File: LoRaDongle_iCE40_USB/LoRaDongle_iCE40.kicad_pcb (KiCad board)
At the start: 4 copper layers, 110 x 45 mm, 129 parts, among them IC1 93LC56BT-I_OT, IC2 ICE40UP5K-UWG30ITR1K, IC3 N25Q032A13ESC40F, J1 USB_A, J2 Conn_01x08, J3 Conn_02x02_Top_Bottom, J4 Jumper, J5 142-0701-801, J6 Conn_01x06, J7 Jumper_NC_Small, J8 Jumper, J9 Conn_02x02_Top_Bottom, SW1 SW_Push, U1 RP550K0001A-TR, U2 FT232H, U3 SX1261IMLTRT, U4 SKY13587-378LF, X1 ECS-2520MV-500-BL-TR, Y1 Crystal_GND24_Small, Y2 Crystal

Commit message: first traces laid
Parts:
- moved C18 1.89 mm to (127.1, 101.4), turned to 0 degrees
- moved C21 1.83 mm to (138.3, 102.5)
- moved C22 1.83 mm to (137.2, 102.5)
- moved R8 1.57 mm to (141.0, 94.7)
- moved C13 1.13 mm to (139.2, 91.0)
- moved C16 1.13 mm to (138.2, 91.0)
- moved C20 0.98 mm to (127.1, 100.4), turned to 0 degrees
- moved C8 0.66 mm to (129.8, 82.5), turned to 0 degrees
- moved C17 0.35 mm to (135.8, 90.2)
- moved C24 0.17 mm to (158.7, 100.9)
- moved C27 0.17 mm to (159.7, 100.9)
- moved C25 0.13 mm to (153.5, 100.9)
- moved C26 0.13 mm to (152.4, 100.9)
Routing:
- net GND: track 0.00 -> 51.1 mm, vias 0 -> 13
- net 3V3: track 0.00 -> 19.0 mm, vias 0 -> 5
- net /USB_Interface/CS#: track 0.00 -> 17.1 mm, vias 0 -> 2
- net /USB_Interface/CLK: track 0.00 -> 14.1 mm, vias 0 -> 2
- net /USB_Interface/VPLL: track 0.00 -> 13.2 mm
- net /USB_Interface/VPHY: track 0.00 -> 13.2 mm
- net /USB_Interface/DATA: track 0.00 -> 8.67 mm
- net Net-(C37-Pad2): track 0.00 -> 7.66 mm
- net /RF Circuitry/DIO2: track 0.00 -> 5.84 mm, vias 0 -> 1
- net Net-(C49-Pad2): track 0.00 -> 5.63 mm
- net /ice40up5k_circuit/ANTENNA_SW: track 0.00 -> 5.27 mm, vias 0 -> 1
- net Net-(C13-Pad1): track 0.00 -> 4.13 mm
- net Net-(C16-Pad1): track 0.00 -> 3.85 mm
- net /USB_Interface/~RESET: track 0.00 -> 3.82 mm
- net /RF Circuitry/VCTL1: track 0.00 -> 3.78 mm
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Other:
- rule trace_min: 0.15 -> 0.1

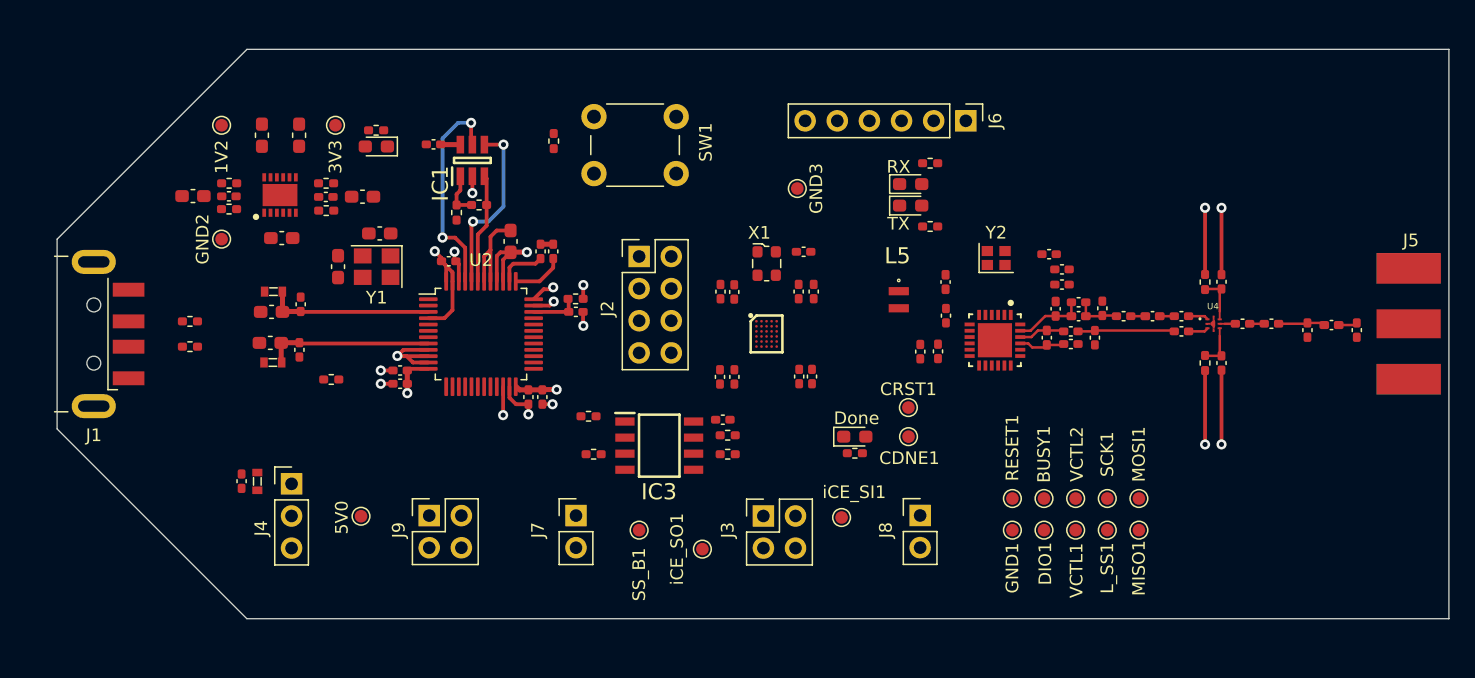
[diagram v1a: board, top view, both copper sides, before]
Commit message: added more traces
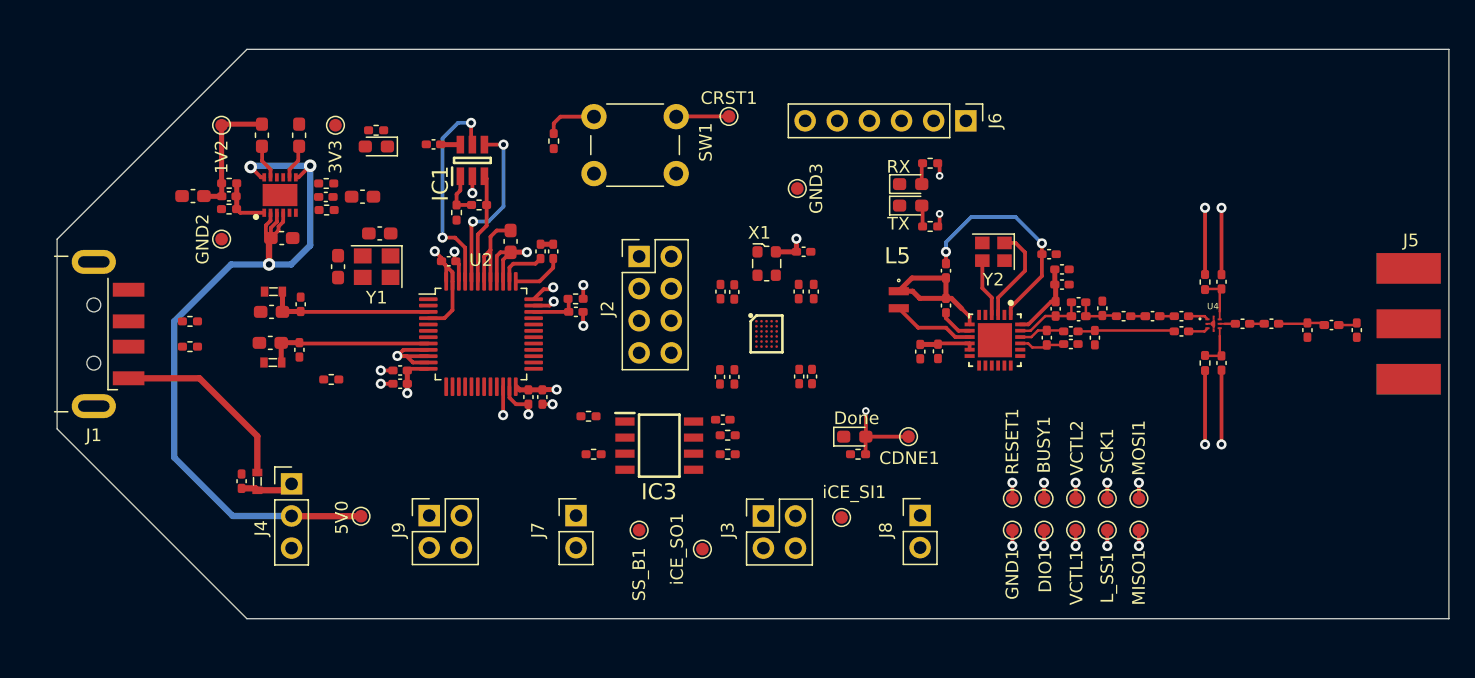
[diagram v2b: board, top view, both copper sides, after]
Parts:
- Y2: value Crystal -> Crystal_GND24; footprint Crystal:Crystal_SMD_2016-4Pin_2.0x1.6mm -> Crystal:Crystal_SMD_2520-4Pin_2.5x2.0mm
- moved CRST1 27.0 mm to (153.1, 80.3)
- moved R4 2.15 mm to (121.3, 85.6)
- moved R5 2.11 mm to (121.3, 87.7)
- moved L3 0.89 mm to (170.2, 92.5)
- moved C42 0.80 mm to (170.2, 95.2)
- moved Y2 0.54 mm to (174.0, 91.0), turned to 180 degrees
- moved R12 0.26 mm to (163.3, 107.0)
- turned R21 to 180 degrees
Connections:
- Y2 pad 1: Net-(U3-Pad4) -> Net-(U3-Pad3)
- Y2 pad 2: Net-(U3-Pad3) -> GND
- Y2 pad 3: (no net) -> Net-(U3-Pad4)
- Y2 pad 4: (no net) -> GND
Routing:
- net +5V: track 0.00 -> 63.7 mm, vias 0 -> 3
- net Net-(C35-Pad1): track 0.00 -> 17.6 mm, vias 0 -> 2
- net /VBUS: track 0.00 -> 14.9 mm
- net /RF Circuitry/VREG: track 0.00 -> 12.8 mm
- net 1V2: track 0.00 -> 10.3 mm
- net /ICE_CRESET: track 0.00 -> 8.38 mm
- net Net-(U3-Pad3): track 0.00 -> 7.76 mm
- net /ICE_CDONE: track 0.00 -> 6.80 mm, vias 0 -> 1
- net Net-(L5-Pad2): track 0.00 -> 6.54 mm
- net /RF Circuitry/VR_PA: track 0.00 -> 6.12 mm
- net Net-(U3-Pad4): track 0.00 -> 4.60 mm
- net RadioPower: track 0.00 -> 4.43 mm
- net Net-(C5-Pad1): track 0.00 -> 4.35 mm
- net /V_USB: track 0.00 -> 4.22 mm
- net GND: track 51.1 -> 55.1 mm, vias 13 -> 14
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
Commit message: breakout of bga part
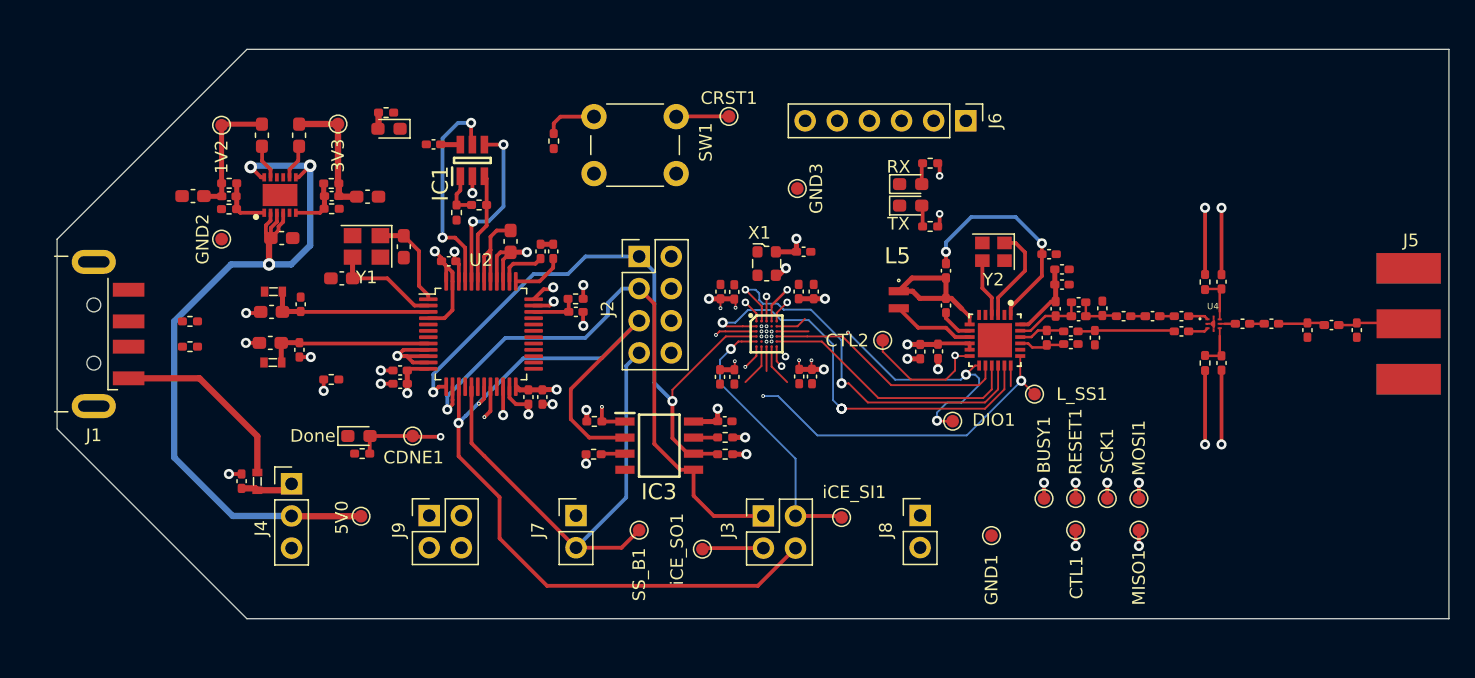
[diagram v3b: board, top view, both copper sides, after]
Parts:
- CTL1: renamed from VCTL1; value VCTL1 -> CTL1
- CTL2: renamed from VCTL2; value VCTL2 -> CTL2
- moved R12 39.2 mm to (124.1, 107.0)
- moved CDNE1 39.2 mm to (128.1, 105.6)
- moved D2 39.2 mm to (123.9, 105.6)
- moved CTL2 19.7 mm to (165.2, 98.0), turned to 90 degrees
- moved L_SS1 12.2 mm to (177.2, 102.2), turned to 180 degrees
- moved DIO1 11.2 mm to (170.8, 104.4), turned to 90 degrees
- moved RESET1 5.00 mm to (180.5, 110.5)
- moved C14 2.17 mm to (127.4, 90.6), turned to 270 degrees
- moved Y1 1.79 mm to (124.5, 90.6)
- moved D1 1.72 mm to (126.2, 81.3)
- moved GND1 1.71 mm to (173.8, 113.4)
- moved R3 1.60 mm to (126.0, 80.0)
- moved C15 0.97 mm to (122.5, 93.1), turned to 180 degrees
- moved R15 0.62 mm to (142.5, 104.4)
- moved C3 0.47 mm to (121.7, 86.6)
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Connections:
- J2 pad 1: /ICE_CRESET -> /SPI_SCK
- J2 pad 2: /ICE_CDONE -> /ICE_CRESET
- J2 pad 3: /SPI_SS -> /SPI_MOSI
- J2 pad 4: /SPI_MISO -> /ICE_CDONE
- J2 pad 5: /SPI_MOSI -> /SPI_MISO
- J2 pad 6: /SPI_SCK -> GND
- J2 pad 7: GND -> /SPI_SS
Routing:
- net /SPI_MISO: track 0.00 -> 72.0 mm, vias 0 -> 1
- net /SPI_SCK: track 1.25 -> 54.4 mm, vias 1 -> 3
- net /SPI_SS: track 0.00 -> 49.9 mm, vias 0 -> 1
- net /SPI_MOSI: track 0.00 -> 47.3 mm, vias 0 -> 1
- net /ICE_CDONE: track 6.80 -> 44.0 mm, vias 1 -> 4
- net /RF Circuitry/LoRa_MOSI: track 1.25 -> 35.0 mm, vias 1 -> 4
- net /ICE_CRESET: track 8.38 -> 41.9 mm, vias 0 -> 1
- net /RF Circuitry/LoRa_MISO: track 1.25 -> 32.5 mm, vias 1 -> 3
- net /RF Circuitry/LoRa_!SS: track 1.25 -> 31.9 mm, vias 1 -> 4
- net /RF Circuitry/DIO1: track 1.25 -> 26.7 mm, vias 1 -> 5
- net /ice40up5k_circuit/iCE_SO: track 0.00 -> 22.7 mm, vias 0 -> 1
- net /ice40up5k_circuit/iCE_SI: track 0.00 -> 22.0 mm, vias 0 -> 1
- net /ice40up5k_circuit/LoRa_~RESET: track 1.25 -> 22.3 mm
- net /RF Circuitry/BUSY: track 1.25 -> 20.6 mm
- net 3V3FPGA: track 0.00 -> 17.2 mm, vias 0 -> 8
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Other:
- net class Default: clearance 0.2 -> 0.1
- rule trace_clearance: 0.2 -> 0.1
- rule via_min_drill: 0.3 -> 0.1
- rule via_min_size: 0.4 -> 0.2

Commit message: added to other traces
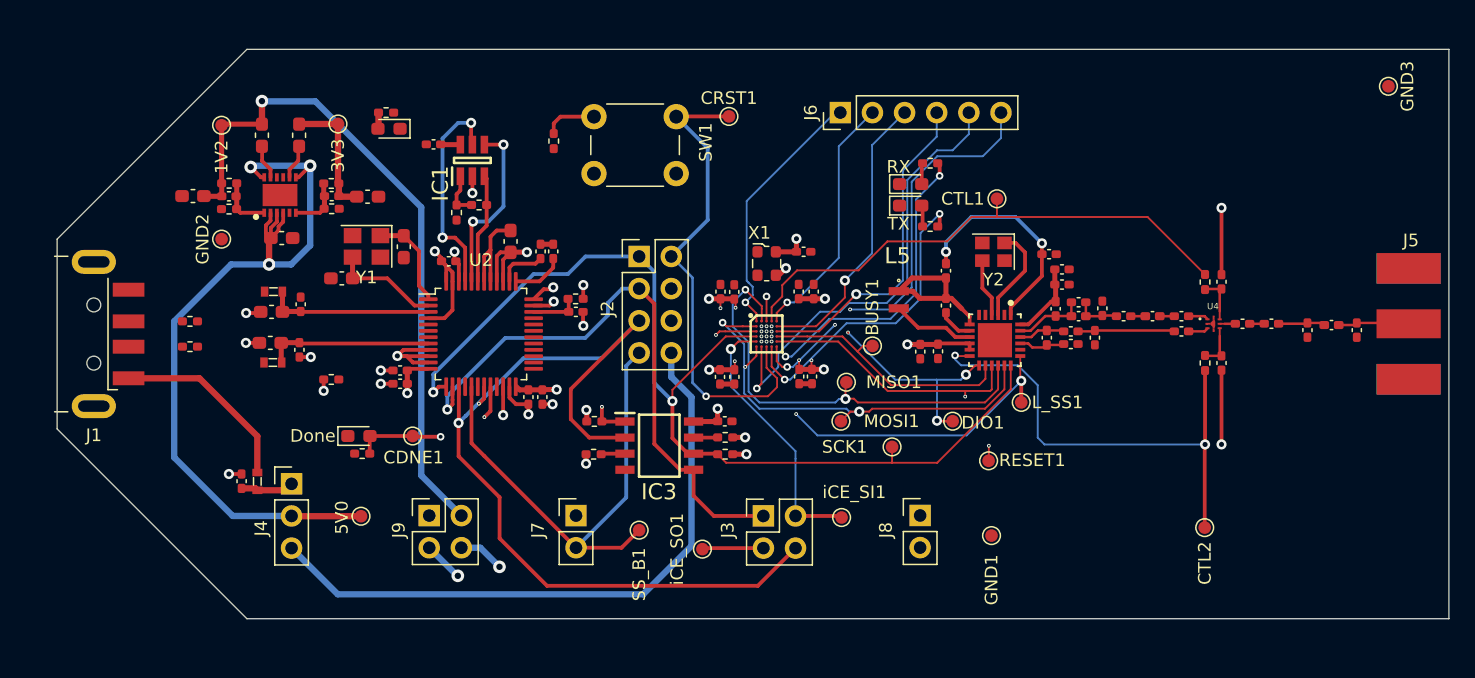
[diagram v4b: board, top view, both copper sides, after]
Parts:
- moved GND3 47.4 mm to (205.2, 77.9)
- moved CTL2 29.4 mm to (190.7, 112.8), turned to 180 degrees
- moved CTL1 26.9 mm to (174.3, 86.8), turned to 90 degrees
- moved MISO1 25.9 mm to (162.4, 101.3), turned to 180 degrees
- moved MOSI1 24.3 mm to (161.9, 104.4), turned to 0 degrees
- moved BUSY1 18.1 mm to (164.4, 98.4)
- moved SCK1 17.5 mm to (166.0, 106.4), turned to 90 degrees
- moved J6 9.94 mm to (161.9, 80.0), turned to 90 degrees
- moved RESET1 7.50 mm to (173.6, 107.5), turned to 90 degrees
- moved L_SS1 1.23 mm to (176.2, 102.9)
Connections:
- net /USB_Interface/~RESET renamed /USB_Interface/~{RESET}
- net /ice40up5k_circuit/ANTENNA_SW renamed /RF Circuitry/ANT_SW
- net /ice40up5k_circuit/LoRa_~RESET renamed /RF Circuitry/~{RESET}
- IC2 pad A5: /ice40up5k_circuit/Pin_3 -> /ice40up5k_circuit/Pin_1
- IC2 pad B5: /ice40up5k_circuit/Pin_4 -> /ice40up5k_circuit/Pin_2
- IC2 pad C5: /ice40up5k_circuit/Pin_5 -> /ice40up5k_circuit/Pin_3
- IC2 pad F2: /ice40up5k_circuit/Pin_2 -> /ice40up5k_circuit/Pin_4
- IC2 pad F5: /ice40up5k_circuit/Pin_1 -> /ice40up5k_circuit/Pin_5
- J1 pad 5: Net-(J1-Pad5) -> unconnected-(J1-Pad5)
- J8 pad 1: 3V3 -> RadioPower
- J8 pad 2: RadioPower -> 3V3
- U2 pad 16: Net-(U2-Pad16) -> unconnected-(U2-Pad16)
- U2 pad 18: Net-(U2-Pad18) -> unconnected-(U2-Pad18)
- U2 pad 21: Net-(U2-Pad21) -> unconnected-(U2-Pad21)
- U2 pad 25: Net-(U2-Pad25) -> unconnected-(U2-Pad25)
- U2 pad 26: Net-(U2-Pad26) -> unconnected-(U2-Pad26)
- U2 pad 27: Net-(U2-Pad27) -> unconnected-(U2-Pad27)
- U2 pad 28: Net-(U2-Pad28) -> unconnected-(U2-Pad28)
- U2 pad 29: Net-(U2-Pad29) -> unconnected-(U2-Pad29)
- U2 pad 30: Net-(U2-Pad30) -> unconnected-(U2-Pad30)
- U2 pad 31: Net-(U2-Pad31) -> unconnected-(U2-Pad31)
- U2 pad 32: Net-(U2-Pad32) -> unconnected-(U2-Pad32)
- U2 pad 33: Net-(U2-Pad33) -> unconnected-(U2-Pad33)
- U4 pad 4: /RF Circuitry/VCTL2 -> /RF Circuitry/CTL2
- U4 pad 6: /RF Circuitry/VCTL1 -> /RF Circuitry/CTL1
- X1 pad 1: Net-(X1-Pad1) -> unconnected-(X1-Pad1)
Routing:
- net 1V2FPGA: track 12.2 -> 80.0 mm, vias 6 -> 7
- net 3V3FPGA: track 17.2 -> 79.7 mm, vias 8 -> 10
- net /V_conn: track 0.00 -> 50.6 mm
- net 1V2: track 10.3 -> 53.8 mm, vias 0 -> 1
- net /ice40up5k_circuit/Pin_4: track 2.47 -> 35.6 mm, vias 0 -> 1
- net /ICE_CRESET: track 41.9 -> 74.9 mm, vias 1 -> 2
- net /RF Circuitry/ANT_SW: track 9.52 -> 42.2 mm, vias 3 -> 0
- net /ice40up5k_circuit/Pin_5: track 2.52 -> 33.5 mm, vias 0 -> 3
- net /SPI_SCK: track 54.4 -> 80.6 mm, vias 3 -> 2
- net /ice40up5k_circuit/Pin_3: track 1.83 -> 26.0 mm
- net /RF Circuitry/DIO2: track 16.0 -> 38.9 mm
- net /RF Circuitry/RX_LED: track 2.71 -> 25.2 mm
- net /RF Circuitry/TX_LED: track 4.38 -> 24.8 mm, vias 1 -> 2
- net /ice40up5k_circuit/Pin_2: track 3.34 -> 22.9 mm, vias 0 -> 1
- net /ice40up5k_circuit/Pin_0: track 1.85 -> 20.6 mm
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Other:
- net class Default removed

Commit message: added copper pours
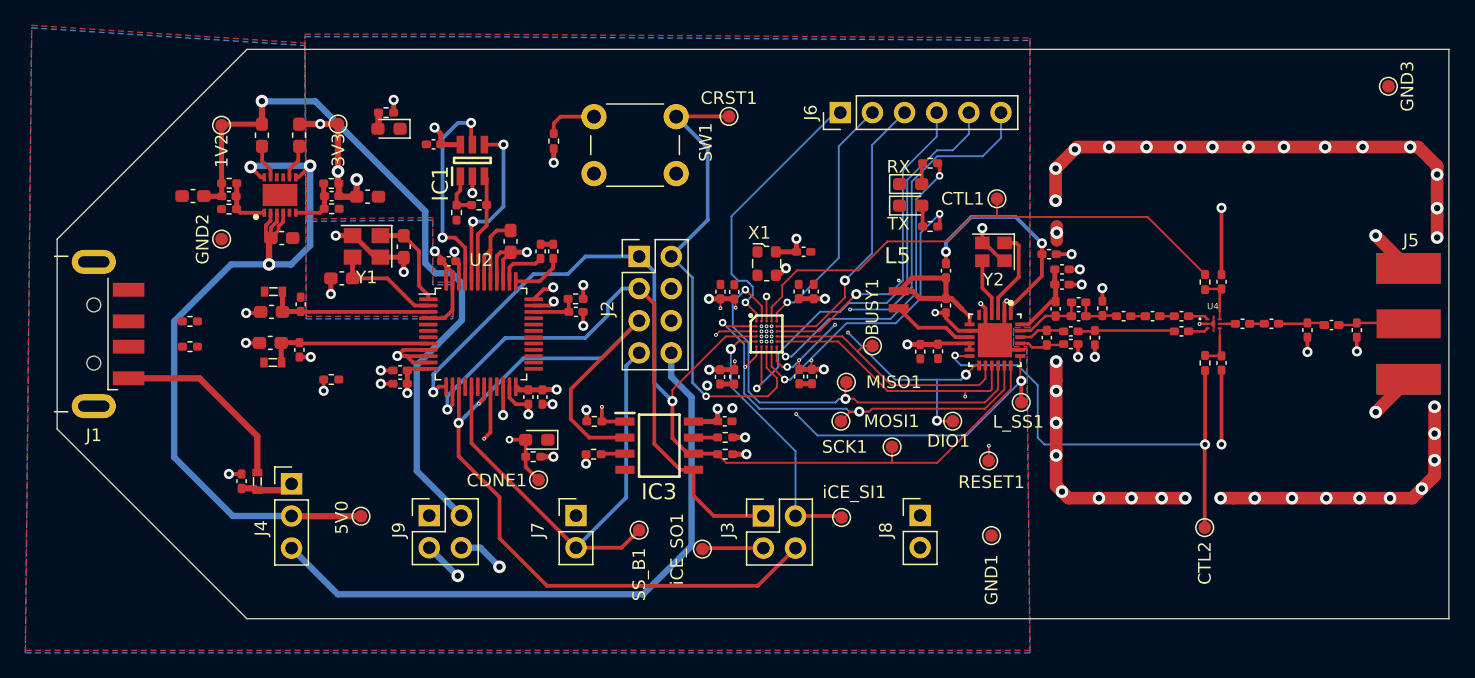
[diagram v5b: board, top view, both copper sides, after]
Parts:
- moved D2 14.1 mm to (137.9, 105.9), turned to 180 degrees
- moved R12 13.5 mm to (137.6, 107.2), turned to 0 degrees
- moved CDNE1 10.5 mm to (138.1, 109.0)
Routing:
- net GND: track 61.1 -> 187.2 mm, vias 20 -> 75
- net 3V3: track 38.5 -> 44.6 mm, vias 11 -> 18
- net /ICE_CDONE: track 44.0 -> 39.5 mm
- net 1V2: track 53.8 -> 57.6 mm
- net /ICE_CRESET: track 74.9 -> 77.7 mm
- net /ice40up5k_circuit/Pin_0: track 20.6 -> 22.0 mm
- added copper zone on In2.Cu, net 3V3
- added copper zone on B.Cu, net GND
- added copper zone on F.Cu, net GND
- added copper zone on In1.Cu, net GND
